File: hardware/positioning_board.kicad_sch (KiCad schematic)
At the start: 30 parts, among them J1 4P4C, J2 USB_C_Receptacle_USB2.0_16P, J3 Conn_01x04, J4 Conn_01x05, J5 Conn_01x05, Q1 MMBT3904, Q2 MMBT3904, SW1 SW_Push, SW2 SW_Push, U1 SN65HVD1782DR, U2 CH340K, U3 ESP32-S3-WROOM-1, U4 LSM6DS3

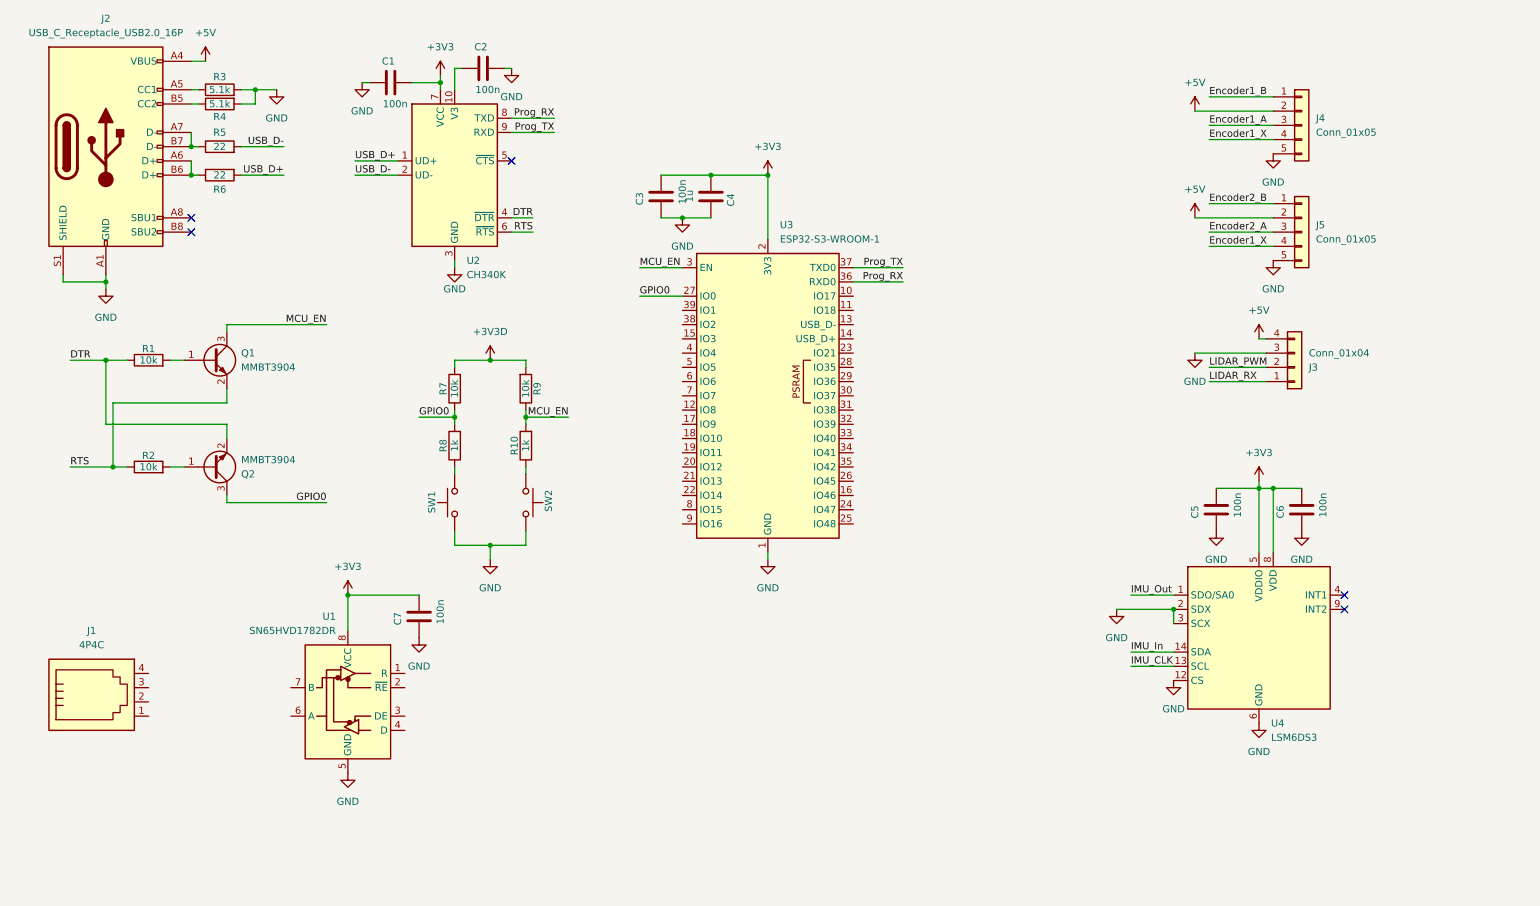
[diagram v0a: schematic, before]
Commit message: Update positioning_board.kicad_sch
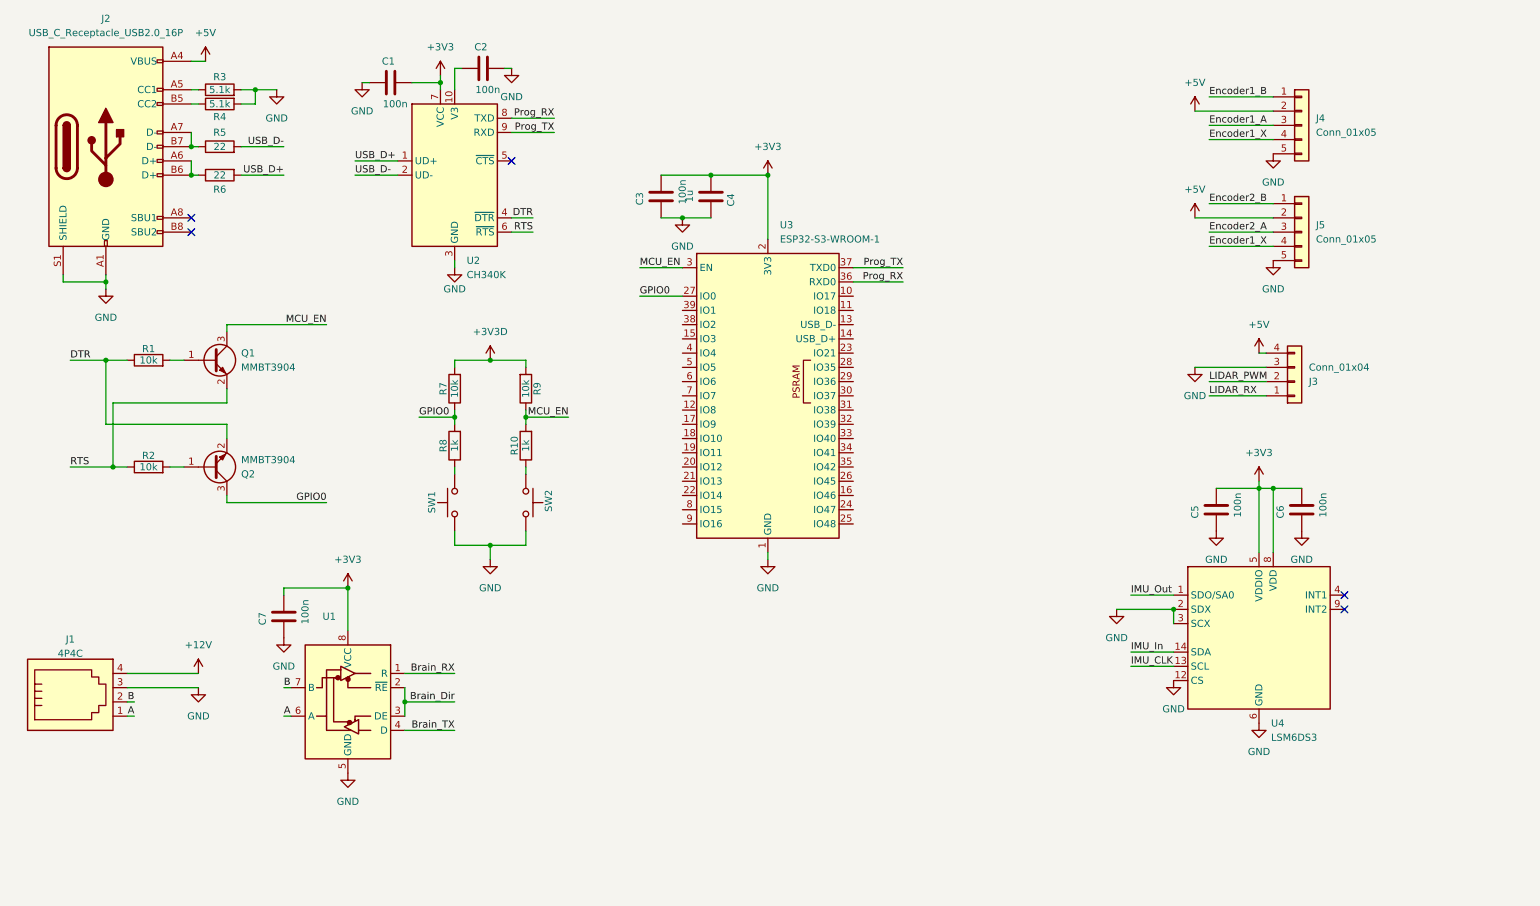
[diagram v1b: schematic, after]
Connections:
- net GND: now also J1.3
- net A: now reaches J1.1
- net A: now also U1.6 (A)
- net B: now reaches J1.2
- net B: now also U1.7 (B)
- net +12V: now reaches J1.4
- net Brain_RX: now reaches U1.1 (R)
- net Brain_Dir: now reaches U1.2 (~{RE})
- net Brain_Dir: now also U1.3 (DE)
- net Brain_TX: now reaches U1.4 (D)
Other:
- moved on the sheet: C7, J1, J3

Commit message: feat: draft layout
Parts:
- added C10: 100n, Capacitor_SMD:C_0603_1608Metric, symbol Device:C
- added C11, C12, C14: 22u, Capacitor_SMD:C_0603_1608Metric, symbol Device:C
- added C13, C8, C9: 10u, Capacitor_SMD:C_0603_1608Metric, symbol Device:C
- added D1, D2: SS24, Diode_SMD:D_SMA, symbol Diode:SS24
- added H1: MountingHole, MountingHole:MountingHole_3.2mm_M3, symbol Mechanical:MountingHole
- added L1: 3.3u, Inductor_SMD:L_Changjiang_FXL0630, symbol Device:L
- added R11: 10k, Resistor_SMD:R_0603_1608Metric, symbol Device:R
- added R12: 56.2k, Resistor_SMD:R_0603_1608Metric, symbol Device:R
- added U5: TPS563200, Package_TO_SOT_SMD:SOT-23-6, symbol Regulator_Switching:TPS563200
- added U7: AMS1117-3.3, Package_TO_SOT_SMD:SOT-223-3_TabPin2, symbol Regulator_Linear:AMS1117-3.3
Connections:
- net +3V3D is gone; now on net +3V3: R7.2, R9.2
- net +12V: now also C8.2, C9.2, U5.3 (VIN), U5.5 (EN)
- net +3V3: now also C14.2, U7.2 (VO)
- net +5V: now also C13.2, D1.1 (K), D2.1 (K), U7.3 (VI); no longer J2.A4 (VBUS), J2.A9 (VBUS), J2.B4 (VBUS), J2.B9 (VBUS)
- net Brain_Dir: now also U3.12 (IO8)
- net Brain_RX: now also U3.11 (IO18)
- net Brain_TX: now also U3.10 (IO17)
- net Encoder1_A: now also U3.8 (IO15)
- net Encoder1_B: now also U3.7 (IO7)
- net Encoder1_X: now also U3.9 (IO16); no longer J5.4 (Pin_4)
- net Encoder2_A: now also U3.32 (IO39)
- net Encoder2_B: now also U3.31 (IO38)
- net GND: now also C11.1, C12.1, C13.1, C14.1, C8.1, C9.1, R11.1, U5.1 (GND), U7.1 (GND); no longer U4.12 (CS)
- net IMU_CLK: now also U3.20 (IO12)
- net IMU_In: now also U3.19 (IO11)
- net IMU_Out: now also U3.21 (IO13)
- net LIDAR_PWM: now also U3.25 (IO48)
- net LIDAR_RX: now also U3.24 (IO47)
- net IMU_CS: now reaches U3.18 (IO10)
- net IMU_CS: now also U4.12 (CS)
- net Encoder2_X: now reaches U3.33 (IO40)
- net Encoder2_X: now also J5.4 (Pin_4)
- new net: C10.2, L1.1, U5.2 (SW)
- new net: R11.2, R12.1, U5.4 (VFB)
- new net: C10.1, U5.6 (VBST)
- new net: D1.2 (A), J2.A4 (VBUS), J2.A9 (VBUS), J2.B4 (VBUS), J2.B9 (VBUS)
- new net: C11.2, C12.2, D2.2 (A), L1.2, R12.2
- no-connect marks 5 -> 23

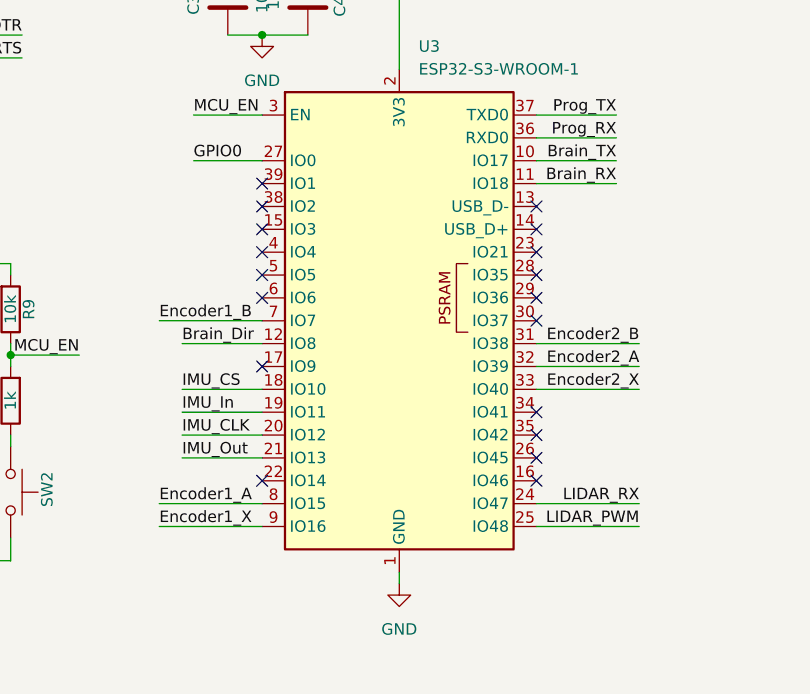
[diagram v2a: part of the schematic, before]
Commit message: reroute lidar pins
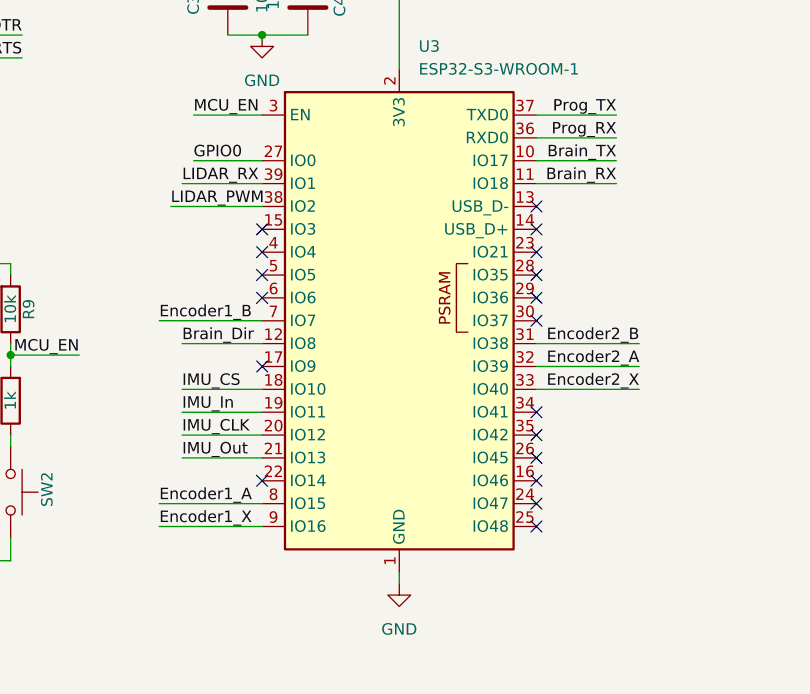
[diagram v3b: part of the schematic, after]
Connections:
- net LIDAR_PWM: now also U3.38 (IO2); no longer U3.25 (IO48)
- net LIDAR_RX: now also U3.39 (IO1); no longer U3.24 (IO47)
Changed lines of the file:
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@@
+	)
+	(no_connect
+		(at 166.37 104.14)
 	)
 	(no_connect
@@
 	)
 	(no_connect
-		(at 135.89 68.58)
-	)
-	(no_connect
 		(at 166.37 81.28)
 	)
@@
 	)
 	(no_connect
-		(at 135.89 71.12)
-	)
-	(no_connect
 		(at 166.37 76.2)
 	)
@@
 	)
 	(no_connect
+		(at 166.37 106.68)
+	)
+	(no_connect
 		(at 135.89 81.28)
 	)
@@
 	(wire
 		(pts
-			(xy 177.8 104.14) (xy 166.37 104.14)
-		)
-		(stroke
-			(width 0)
-			(type default)
-		)
-	)
-	(wire
-		(pts
 			(xy 92.71 26.67) (xy 92.71 27.94)
 		)
@@
 	(wire
 		(pts
+			(xy 127 68.58) (xy 135.89 68.58)
+		)
+		(stroke
+			(width 0)
+			(type default)
+		)
+	)
+	(wire
+		(pts
 			(xy 54.61 71.12) (xy 54.61 72.39)
 		)
@@
 	(wire
 		(pts
-			(xy 177.8 106.68) (xy 166.37 106.68)
-		)
-		(stroke
-			(width 0)
-			(type default)
-		)
-	)
-	(wire
-		(pts
 			(xy 170.18 149.86) (xy 172.72 149.86)
 		)
@@
 		(pts
 			(xy 64.77 39.37) (xy 57.15 39.37)
+		)
+		(stroke
+			(width 0)
+			(type default)
+		)
+	)
+	(wire
+		(pts
+			(xy 125.73 71.12) (xy 135.89 71.12)
 		)
 		(stroke
@@
 		)
 	)
+	(label "LIDAR_PWM"
+		(at 125.73 71.12 0)
+		(effects
+			(font
+				(size 1.27 1.27)
+			)
+			(justify left bottom)
+		)
+	)
 	(label "IMU_CS"
 		(at 127 91.44 0)
@@
 		)
 	)
-	(label "LIDAR_PWM"
-		(at 177.8 106.68 180)
-		(effects
-			(font
-				(size 1.27 1.27)
-			)
-			(justify right bottom)
-		)
-	)
-	(label "LIDAR_RX"
-		(at 177.8 104.14 180)
-		(effects
-			(font
-				(size 1.27 1.27)
-			)
-			(justify right bottom)
-		)
-	)
 	(label "MCU_EN"
 		(at 72.39 71.12 180)
@@
 		(effects
 			(font
+				(size 1.27 1.27)
+			)
+			(justify left bottom)
+		)
+	)
+	(label "LIDAR_RX"
+		(at 127 68.58 0)
+		(effects
+			(font

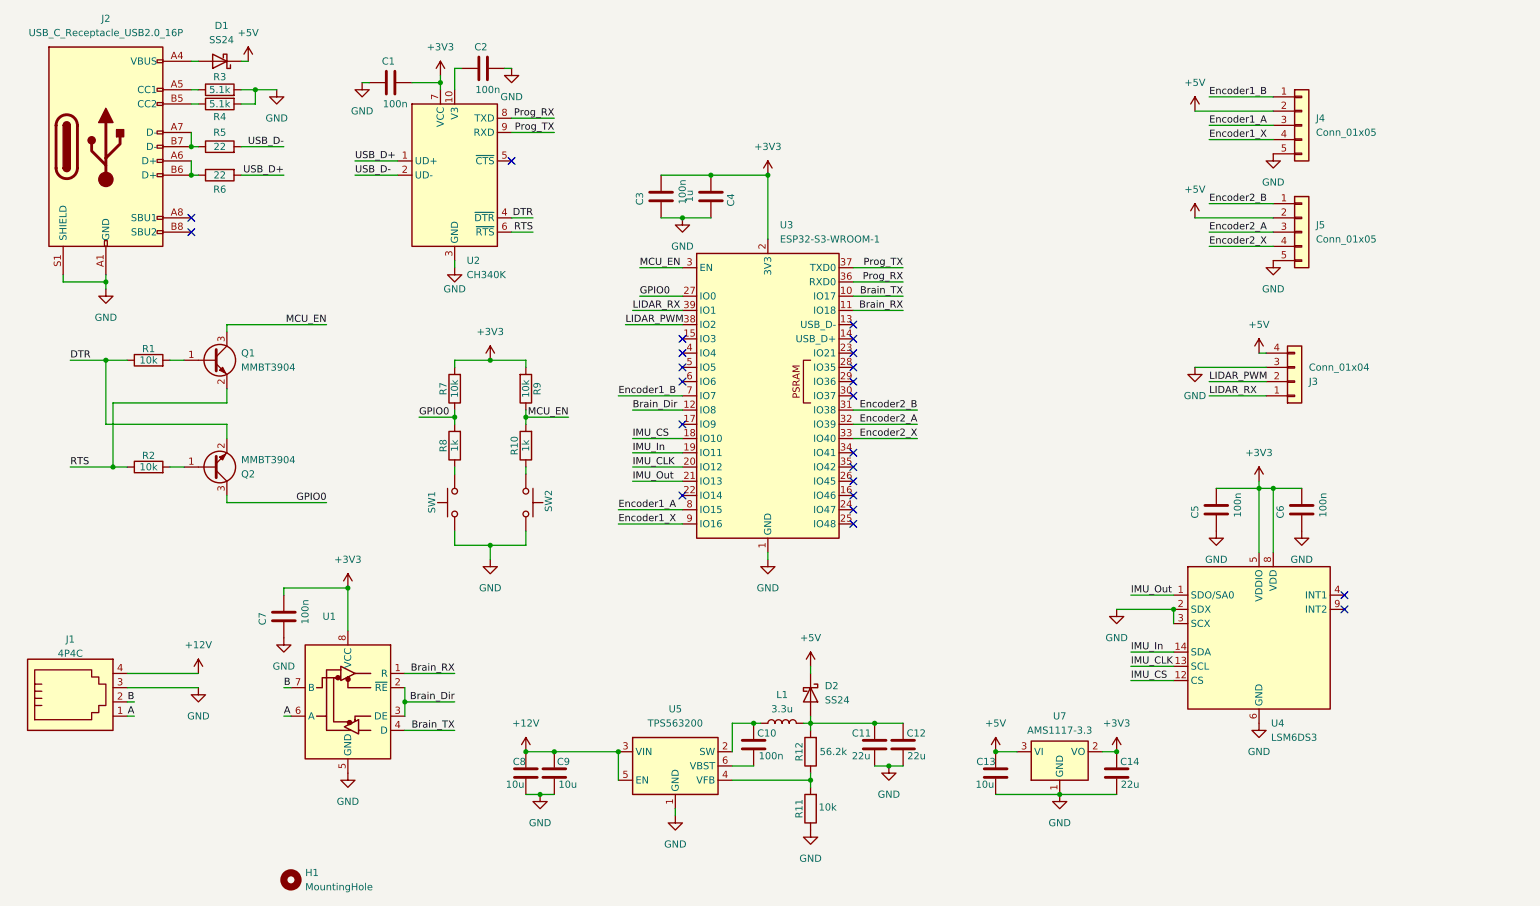
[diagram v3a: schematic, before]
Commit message: reroute some pins
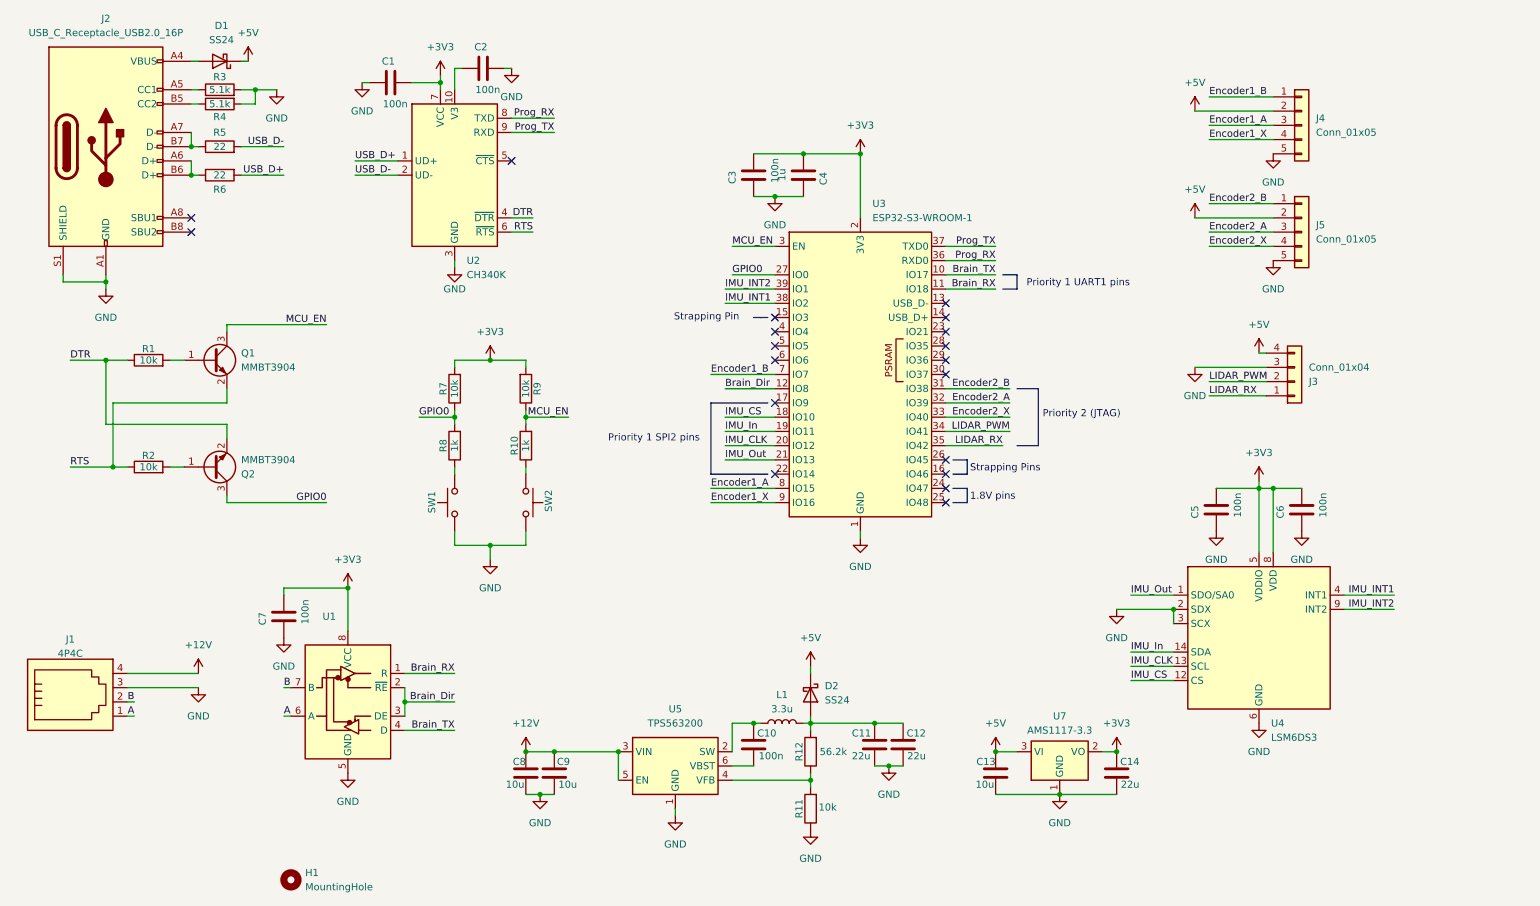
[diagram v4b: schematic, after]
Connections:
- net LIDAR_PWM: now also U3.34 (IO41); no longer U3.38 (IO2)
- net LIDAR_RX: now also U3.35 (IO42); no longer U3.39 (IO1)
- net IMU_INT1: now reaches U4.4 (INT1)
- net IMU_INT1: now also U3.38 (IO2)
- net IMU_INT2: now reaches U4.9 (INT2)
- net IMU_INT2: now also U3.39 (IO1)
- no-connect marks 23 -> 19
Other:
- note added: "1.8V pins"
- note added: "Priority 1 SPI2 pins"
- note added: "Priority 1 UART1 pins"
- note added: "Priority 2 (JTAG)"
- note added: "Strapping Pin"
- note added: "Strapping Pins"
- moved on the sheet: C3, C4, U3
